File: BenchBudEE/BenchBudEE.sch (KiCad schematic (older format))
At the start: 0 parts

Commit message: LED driver schematic
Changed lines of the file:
@@
 Sheet 1 9
 Title ""
-Date "13 feb 2014"
+Date "16 feb 2014"
 Rev ""
 Comp ""
@@
 F0 "LED" 50
 F1 "LED.sch" 50
-F2 "EN" I L 7400 4750 60
-F3 "FREQ" I L 7400 4950 60
-F4 "STRING+" O R 8500 4750 60
-F5 "STRING-" I R 8500 4950 60
+F2 "STRING+" O R 8500 4750 60
+F3 "STRING-" I R 8500 4950 60
+F4 "LED_EN_PWM" I L 7400 4850 60
 $EndSheet
 $Sheet

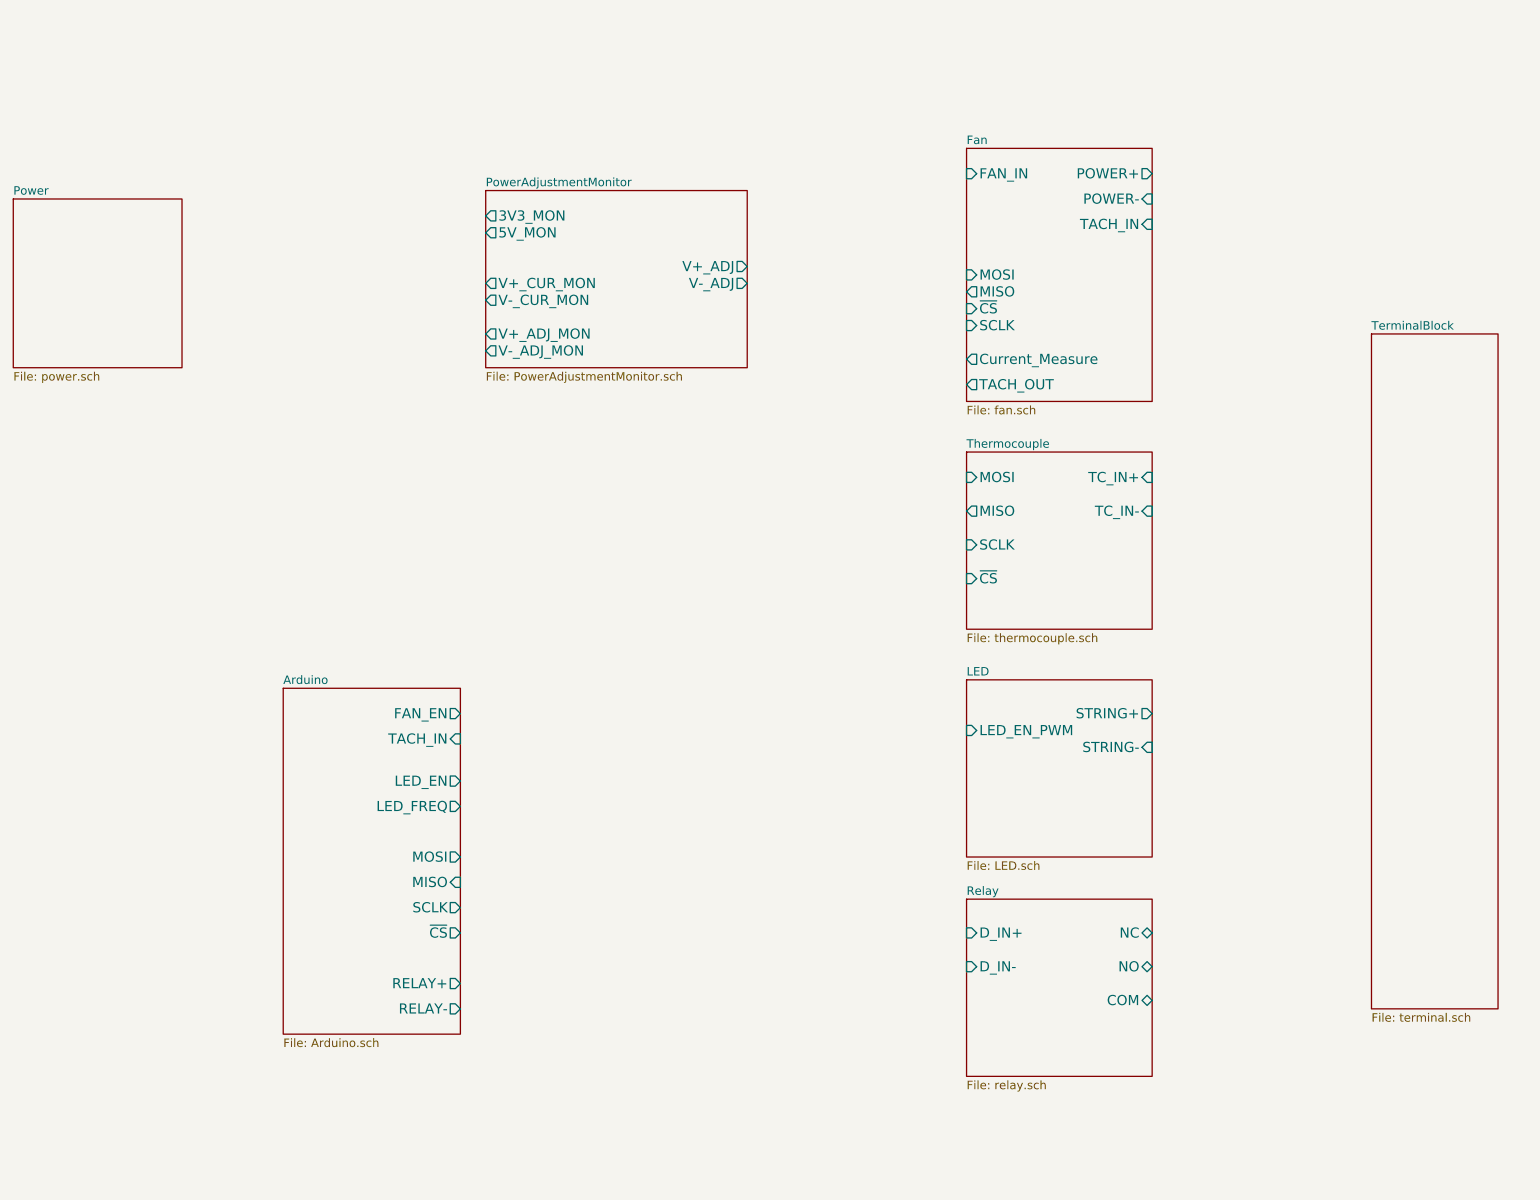
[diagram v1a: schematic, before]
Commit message: arduino schematic and interconnection
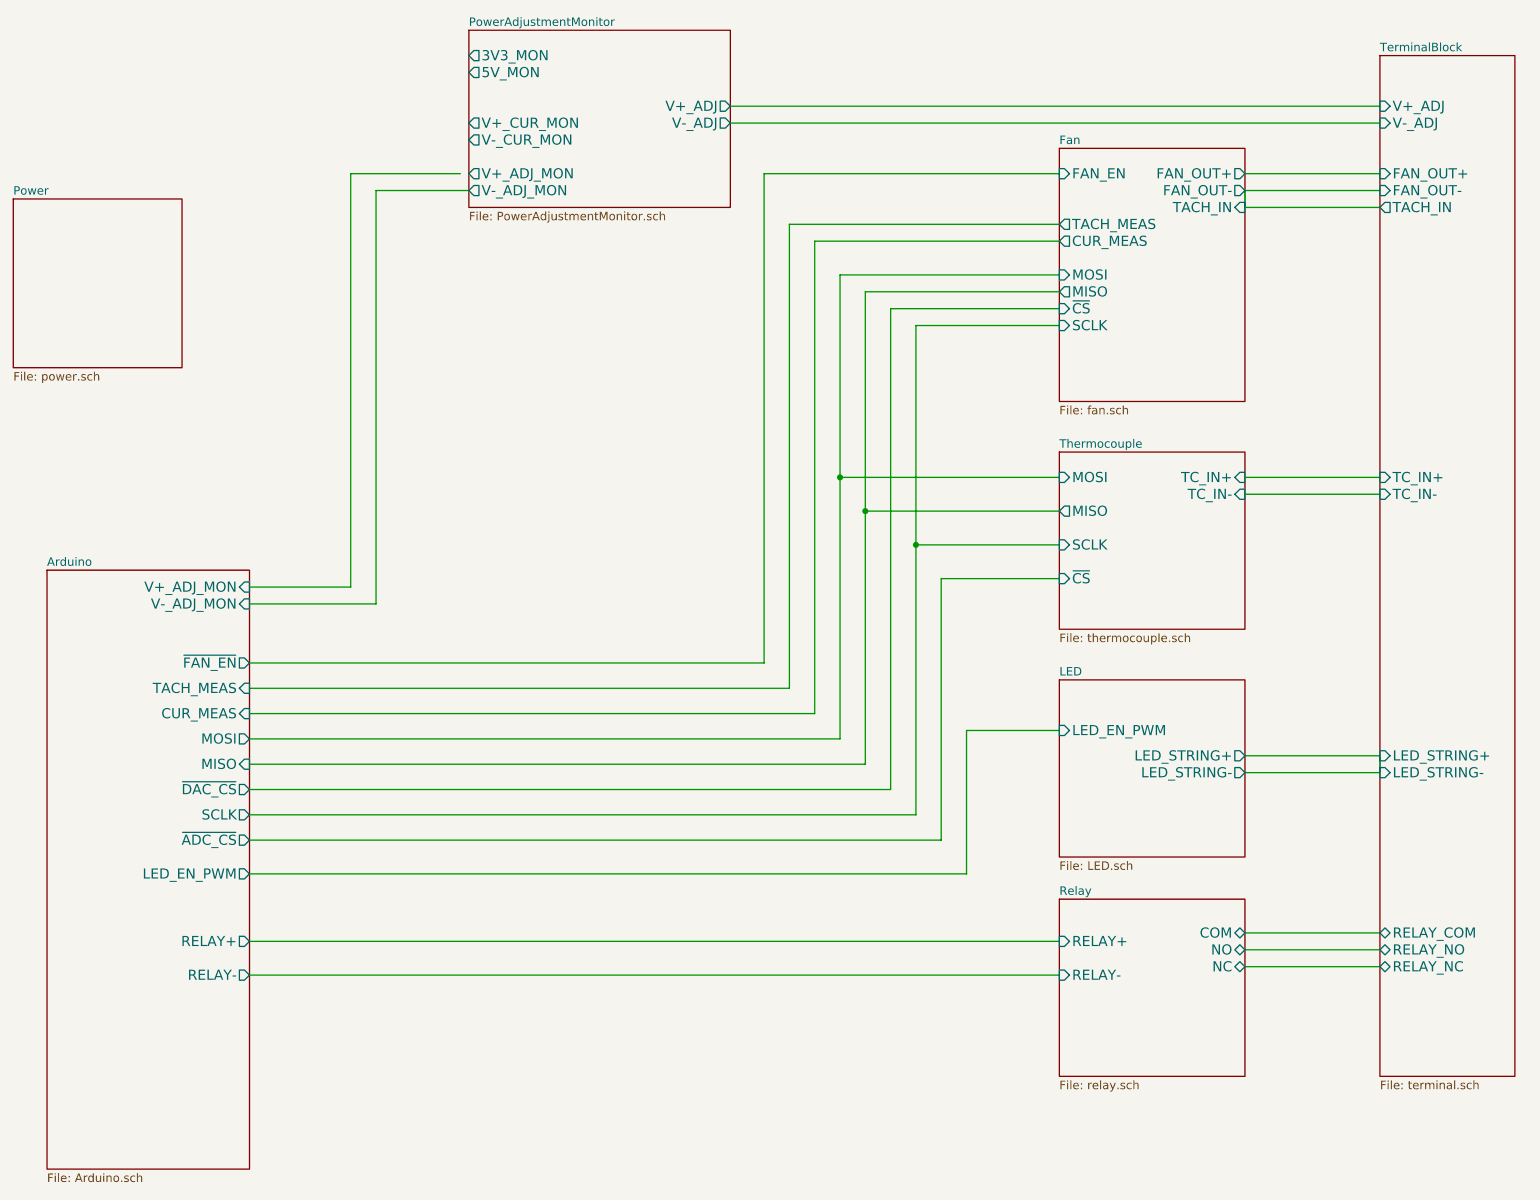
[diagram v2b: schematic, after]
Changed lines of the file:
@@
 Sheet 1 9
 Title ""
-Date "16 feb 2014"
+Date "17 feb 2014"
 Rev ""
 Comp ""
@@
 $EndDescr
 $Sheet
-S 3350 4600 1050 2050
+S 1950 3900 1200 3550
 U 52F19A0B
 F0 "Arduino" 50
 F1 "Arduino.sch" 50
-F2 "RELAY+" O R 4400 6350 60
-F3 "RELAY-" O R 4400 6500 60
-F4 "MOSI" O R 4400 5600 60
-F5 "MISO" I R 4400 5750 60
-F6 "SCLK" O R 4400 5900 60
-F7 "~CS" O R 4400 6050 60
-F8 "LED_EN" O R 4400 5150 60
-F9 "LED_FREQ" O R 4400 5300 60
-F10 "FAN_EN" O R 4400 4750 60
-F11 "TACH_IN" I R 4400 4900 60
+F2 "RELAY+" O R 3150 6100 60
+F3 "RELAY-" O R 3150 6300 60
+F4 "MOSI" O R 3150 4900 60
+F5 "MISO" I R 3150 5050 60
+F6 "SCLK" O R 3150 5350 60
+F7 "TACH_MEAS" I R 3150 4600 60
+F8 "~FAN_EN" O R 3150 4450 60
+F9 "CUR_MEAS" I R 3150 4750 60
+F10 "V+_ADJ_MON" I R 3150 4000 60
+F11 "V-_ADJ_MON" I R 3150 4100 60
+F12 "LED_EN_PWM" O R 3150 5700 60
+F13 "~DAC_CS" O R 3150 5200 60
+F14 "~ADC_CS" O R 3150 5500 60
 $EndSheet
 $Sheet
@@
 $EndSheet
 $Sheet
-S 7400 4550 1100 1050
+S 7950 4550 1100 1050
 U 52F19A48
 F0 "LED" 50
 F1 "LED.sch" 50
-F2 "STRING+" O R 8500 4750 60
-F3 "STRING-" I R 8500 4950 60
-F4 "LED_EN_PWM" I L 7400 4850 60
-$EndSheet
-$Sheet
-S 9800 2500 750  4000
+F2 "LED_EN_PWM" I L 7950 4850 60
+F3 "LED_STRING+" O R 9050 5000 60
+F4 "LED_STRING-" O R 9050 5100 60
+$EndSheet
+$Sheet
+S 7950 3200 1100 1050
+U 52F19AE5
+F0 "Thermocouple" 50
+F1 "thermocouple.sch" 50
+F2 "MOSI" I L 7950 3350 60
+F3 "MISO" O L 7950 3550 60
+F4 "SCLK" I L 7950 3750 60
+F5 "~CS" I L 7950 3950 60
+F6 "TC_IN+" I R 9050 3350 60
+F7 "TC_IN-" I R 9050 3450 60
+$EndSheet
+$Sheet
+S 7950 5850 1100 1050
+U 52F19A58
+F0 "Relay" 50
+F1 "relay.sch" 50
+F2 "NC" B R 9050 6250 60
+F3 "NO" B R 9050 6150 60
+F4 "COM" B R 9050 6050 60
+F5 "RELAY+" I L 7950 6100 60
+F6 "RELAY-" I L 7950 6300 60
+$EndSheet
+$Sheet
+S 7950 1400 1100 1500
+U 52F19A3C
+F0 "Fan" 50
+F1 "fan.sch" 50
+F2 "TACH_IN" I R 9050 1750 60
+F3 "MOSI" I L 7950 2150 60
+F4 "MISO" O L 7950 2250 60
+F5 "~CS" I L 7950 2350 60
+F6 "SCLK" I L 7950 2450 60
+F7 "FAN_OUT+" O R 9050 1550 60
+F8 "TACH_MEAS" O L 7950 1850 60
+F9 "FAN_EN" I L 7950 1550 60
+F10 "FAN_OUT-" O R 9050 1650 60
+F11 "CUR_MEAS" O L 7950 1950 60
+$EndSheet
+$Sheet
+S 4450 700  1550 1050
+U 52FADC37
+F0 "PowerAdjustmentMonitor" 50
+F1 "PowerAdjustmentMonitor.sch" 50
+F2 "V+_ADJ" O R 6000 1150 60
+F3 "V-_ADJ" O R 6000 1250 60
+F4 "3V3_MON" O L 4450 850 60
+F5 "5V_MON" O L 4450 950 60
+F6 "V+_ADJ_MON" O L 4450 1550 60
+F7 "V-_ADJ_MON" O L 4450 1650 60
+F8 "V+_CUR_MON" O L 4450 1250 60
+F9 "V-_CUR_MON" O L 4450 1350 60
+$EndSheet
+Wire Wire Line
+	9050 6250 9850 6250
+Wire Wire Line
+	9050 6150 9850 6150
+Wire Wire Line
+	9050 6050 9850 6050
+Wire Wire Line
+	9050 5000 9850 5000
+Wire Wire Line
+	9050 5100 9850 5100
+$Sheet
+S 9850 850  800  6050
 U 52F19A64
 F0 "TerminalBlock" 50
 F1 "terminal.sch" 50
-$EndSheet
-$Sheet
-S 7400 3200 1100 1050
-U 52F19AE5
-F0 "Thermocouple" 50
-F1 "thermocouple.sch" 50
-F2 "MOSI" I L 7400 3350 60
-F3 "MISO" O L 7400 3550 60
-F4 "SCLK" I L 7400 3750 60
-F5 "~CS" I L 7400 3950 60
-F6 "TC_IN+" I R 8500 3350 60
-F7 "TC_IN-" I R 8500 3550 60
-$EndSheet
-$Sheet
-S 7400 5850 1100 1050
-U 52F19A58
-F0 "Relay" 50
-F1 "relay.sch" 50
-F2 "D_IN+" I L 7400 6050 60
-F3 "D_IN-" I L 7400 6250 60
-F4 "NC" B R 8500 6050 60
-F5 "NO" B R 8500 6250 60
-F6 "COM" B R 8500 6450 60
-$EndSheet
-$Sheet
-S 7400 1400 1100 1500
-U 52F19A3C
-F0 "Fan" 50
-F1 "fan.sch" 50
-F2 "POWER+" O R 8500 1550 60
-F3 "POWER-" I R 8500 1700 60
-F4 "TACH_IN" I R 8500 1850 60
-F5 "TACH_OUT" O L 7400 2800 60
-F6 "FAN_IN" I L 7400 1550 60
-F7 "Current_Measure" O L 7400 2650 60
-F8 "MOSI" I L 7400 2150 60
-F9 "MISO" O L 7400 2250 60
-F10 "~CS" I L 7400 2350 60
-F11 "SCLK" I L 7400 2450 60
-$EndSheet
-$Sheet
-S 4550 1650 1550 1050
-U 52FADC37
-F0 "PowerAdjustmentMonitor" 50
-F1 "PowerAdjustmentMonitor.sch" 50
-F2 "V+_ADJ" O R 6100 2100 60
-F3 "V-_ADJ" O R 6100 2200 60
-F4 "3V3_MON" O L 4550 1800 60
-F5 "5V_MON" O L 4550 1900 60
-F6 "V+_ADJ_MON" O L 4550 2500 60
-F7 "V-_ADJ_MON" O L 4550 2600 60
-F8 "V+_CUR_MON" O L 4550 2200 60
-F9 "V-_CUR_MON" O L 4550 2300 60
-$EndSheet
+F2 "V+_ADJ" I L 9850 1150 60
+F3 "V-_ADJ" I L 9850 1250 60
+F4 "FAN_OUT+" I L 9850 1550 60
+F5 "FAN_OUT-" I L 9850 1650 60
+F6 "LED_STRING+" I L 9850 5000 60
+F7 "LED_STRING-" I L 9850 5100 60
+F8 "TC_IN+" I L 9850 3350 60
+F9 "TC_IN-" I L 9850 3450 60
+F10 "RELAY_COM" B L 9850 6050 60
+F11 "RELAY_NO" B L 9850 6150 60
+F12 "RELAY_NC" B L 9850 6250 60
+F13 "TACH_IN" O L 9850 1750 60
+$EndSheet
+Wire Wire Line
+	9850 5100 9850 5000
+Wire Wire Line
+	9850 3350 9050 3350
+Wire Wire Line
+	9050 3450 9850 3450
+Wire Wire Line
+	9050 1750 9850 1750
+Wire Wire Line
+	9050 1750 9050 1650
+Wire Wire Line
+	9050 1650 9850 1650
+Wire Wire Line
+	9050 1550 9850 1550
+Wire Wire Line
+	6000 1150 9850 1150
+Wire Wire Line
+	9850 1250 6000 1250
+Wire Wire Line
+	3150 4450 6200 4450
+Wire Wire Line
+	6200 4450 6200 1550
+Wire Wire Line
+	6200 1550 7950 1550
+Wire Wire Line
+	6650 4900 3150 4900
+Wire Wire Line
+	6650 2150 6650 3350
+Wire Wire Line
+	6650 3350 6650 4900
+Wire Wire Line
+	6650 2150 7950 2150
+Wire Wire Line
+	3150 5050 6800 5050
+Wire Wire Line
+	6800 5050 6800 3550
+Wire Wire Line
+	6800 3550 6800 2250
+Wire Wire Line
+	6800 2250 7950 2250
+Wire Wire Line
+	6950 5200 3150 5200
+Wire Wire Line
+	6950 2350 6950 5200
+Wire Wire Line
+	6950 2350 7950 2350
+Wire Wire Line
+	7950 2450 7100 2450
+Wire Wire Line
+	7100 2450 7100 3750
+Wire Wire Line
+	7100 3750 7100 5350
+Wire Wire Line
+	7100 5350 3150 5350
+Wire Wire Line
+	3150 5700 7400 5700
+Wire Wire Line
+	7400 5700 7400 4850
+Wire Wire Line
+	7400 4850 7950 4850
+Wire Wire Line
+	3150 4600 6350 4600
+Wire Wire Line
+	6350 4600 6350 1850
+Wire Wire Line
+	6350 1850 7950 1850
+Wire Wire Line
+	3150 4750 6500 4750
+Wire Wire Line
+	6500 4750 6500 1950
+Wire Wire Line
+	6500 1950 7950 1950
+Wire Wire Line
+	3150 5500 7250 5500
+Wire Wire Line
+	7250 5500 7250 3950
+Wire Wire Line
+	7250 3950 7950 3950
+Wire Wire Line
+	7950 3750 7100 3750
+Connection ~ 7100 3750
+Wire Wire Line
+	3150 4100 3900 4100
+Wire Wire Line
+	3900 4100 3900 1650
+Wire Wire Line
+	3900 1650 4450 1650
+Wire Wire Line
+	4400 1550 3750 1550
+Wire Wire Line
+	3750 1550 3750 4000
+Wire Wire Line
+	3750 4000 3150 4000
+Wire Wire Line
+	6800 3550 7950 3550
+Connection ~ 6800 3550
+Wire Wire Line
+	7950 3350 6650 3350
+Connection ~ 6650 3350
+Wire Wire Line
+	7950 6100 3150 6100
+Wire Wire Line
+	7950 6300 3150 6300
 $EndSCHEMATC

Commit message: fan/current supply refactor
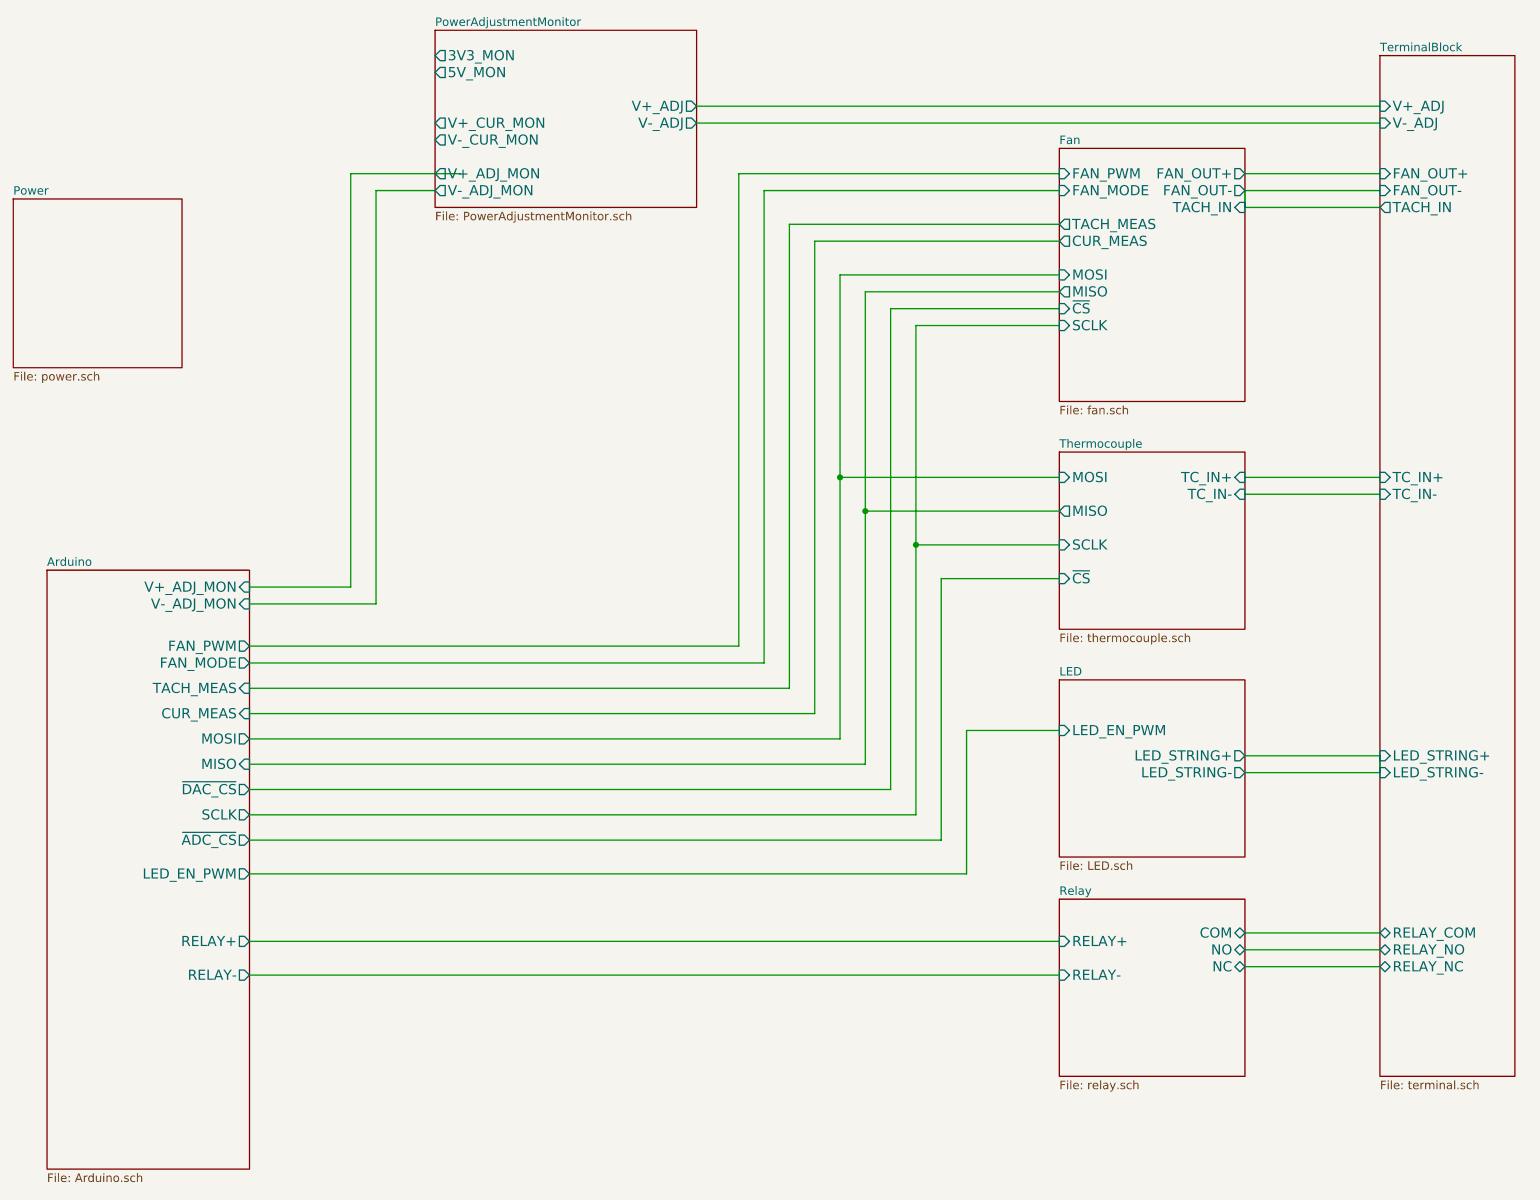
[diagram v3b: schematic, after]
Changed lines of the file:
@@
 F6 "SCLK" O R 3150 5350 60
 F7 "TACH_MEAS" I R 3150 4600 60
-F8 "~FAN_EN" O R 3150 4450 60
-F9 "CUR_MEAS" I R 3150 4750 60
-F10 "V+_ADJ_MON" I R 3150 4000 60
-F11 "V-_ADJ_MON" I R 3150 4100 60
-F12 "LED_EN_PWM" O R 3150 5700 60
-F13 "~DAC_CS" O R 3150 5200 60
-F14 "~ADC_CS" O R 3150 5500 60
+F8 "CUR_MEAS" I R 3150 4750 60
+F9 "V+_ADJ_MON" I R 3150 4000 60
+F10 "V-_ADJ_MON" I R 3150 4100 60
+F11 "LED_EN_PWM" O R 3150 5700 60
+F12 "~DAC_CS" O R 3150 5200 60
+F13 "~ADC_CS" O R 3150 5500 60
+F14 "FAN_PWM" O R 3150 4350 60
+F15 "FAN_MODE" O R 3150 4450 60
 $EndSheet
 $Sheet
@@
 F7 "FAN_OUT+" O R 9050 1550 60
 F8 "TACH_MEAS" O L 7950 1850 60
-F9 "FAN_EN" I L 7950 1550 60
-F10 "FAN_OUT-" O R 9050 1650 60
-F11 "CUR_MEAS" O L 7950 1950 60
-$EndSheet
-$Sheet
-S 4450 700  1550 1050
+F9 "FAN_OUT-" O R 9050 1650 60
+F10 "CUR_MEAS" O L 7950 1950 60
+F11 "FAN_PWM" I L 7950 1550 60
+F12 "FAN_MODE" I L 7950 1650 60
+$EndSheet
+$Sheet
+S 4250 700  1550 1050
 U 52FADC37
 F0 "PowerAdjustmentMonitor" 50
 F1 "PowerAdjustmentMonitor.sch" 50
-F2 "V+_ADJ" O R 6000 1150 60
-F3 "V-_ADJ" O R 6000 1250 60
-F4 "3V3_MON" O L 4450 850 60
-F5 "5V_MON" O L 4450 950 60
-F6 "V+_ADJ_MON" O L 4450 1550 60
-F7 "V-_ADJ_MON" O L 4450 1650 60
-F8 "V+_CUR_MON" O L 4450 1250 60
-F9 "V-_CUR_MON" O L 4450 1350 60
+F2 "V+_ADJ" O R 5800 1150 60
+F3 "V-_ADJ" O R 5800 1250 60
+F4 "3V3_MON" O L 4250 850 60
+F5 "5V_MON" O L 4250 950 60
+F6 "V+_ADJ_MON" O L 4250 1550 60
+F7 "V-_ADJ_MON" O L 4250 1650 60
+F8 "V+_CUR_MON" O L 4250 1250 60
+F9 "V-_CUR_MON" O L 4250 1350 60
 $EndSheet
 Wire Wire Line
@@
 	9050 1550 9850 1550
 Wire Wire Line
-	6000 1150 9850 1150
-Wire Wire Line
-	9850 1250 6000 1250
-Wire Wire Line
-	3150 4450 6200 4450
-Wire Wire Line
-	6200 4450 6200 1550
-Wire Wire Line
-	6200 1550 7950 1550
+	5800 1150 9850 1150
+Wire Wire Line
+	9850 1250 5800 1250
+Wire Wire Line
+	3150 4350 6050 4350
+Wire Wire Line
+	6050 4350 6050 1550
+Wire Wire Line
+	6050 1550 7950 1550
 Wire Wire Line
 	6650 4900 3150 4900
 Wire Wire Line
-	6650 2150 6650 3350
-Wire Wire Line
-	6650 3350 6650 4900
+	6650 2150 6650 4900
 Wire Wire Line
 	6650 2150 7950 2150
 Wire Wire Line
-	3150 5050 6800 5050
-Wire Wire Line
-	6800 5050 6800 3550
-Wire Wire Line
-	6800 3550 6800 2250
+	6800 5050 3150 5050
+Wire Wire Line
+	6800 2250 6800 5050
 Wire Wire Line
 	6800 2250 7950 2250
@@
 	7950 2450 7100 2450
 Wire Wire Line
-	7100 2450 7100 3750
-Wire Wire Line
-	7100 3750 7100 5350
+	7100 2450 7100 5350
 Wire Wire Line
 	7100 5350 3150 5350
@@
 	3900 4100 3900 1650
 Wire Wire Line
-	3900 1650 4450 1650
+	3900 1650 4250 1650
 Wire Wire Line
 	4400 1550 3750 1550
@@
 Wire Wire Line
 	7950 6300 3150 6300
+Wire Wire Line
+	3150 4450 6200 4450
+Wire Wire Line
+	6200 4450 6200 1650
+Wire Wire Line
+	6200 1650 7950 1650
 $EndSCHEMATC
